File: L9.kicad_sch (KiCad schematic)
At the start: 38 parts

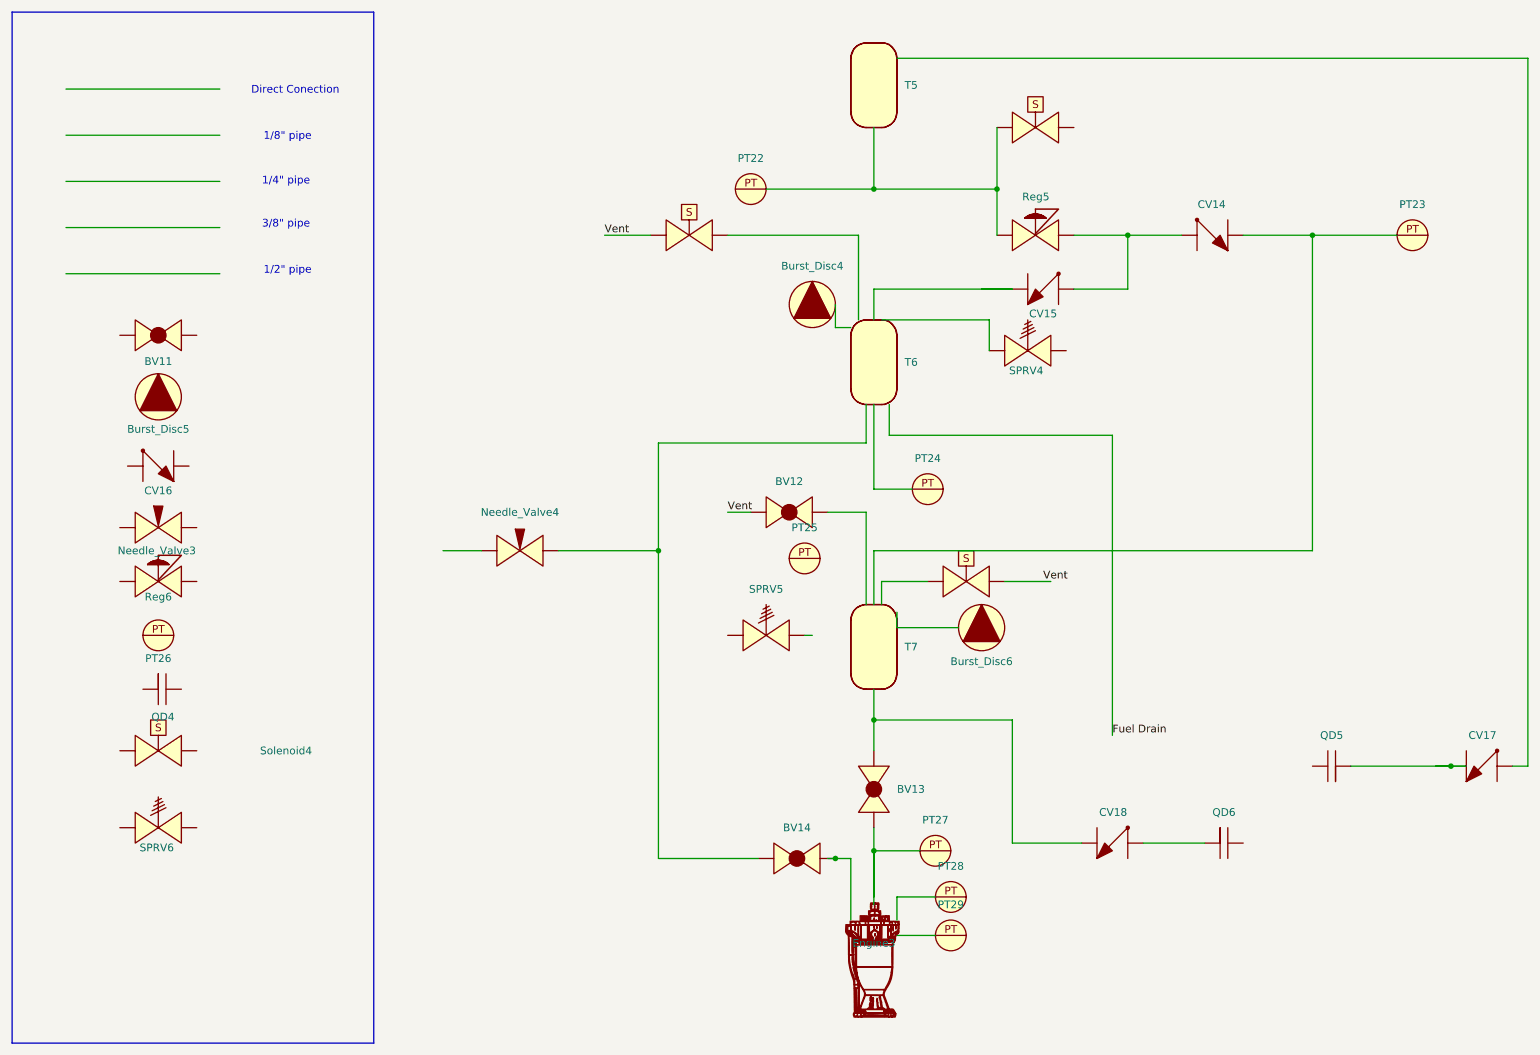
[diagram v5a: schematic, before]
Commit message: Added Igniter + Hopper Engine test
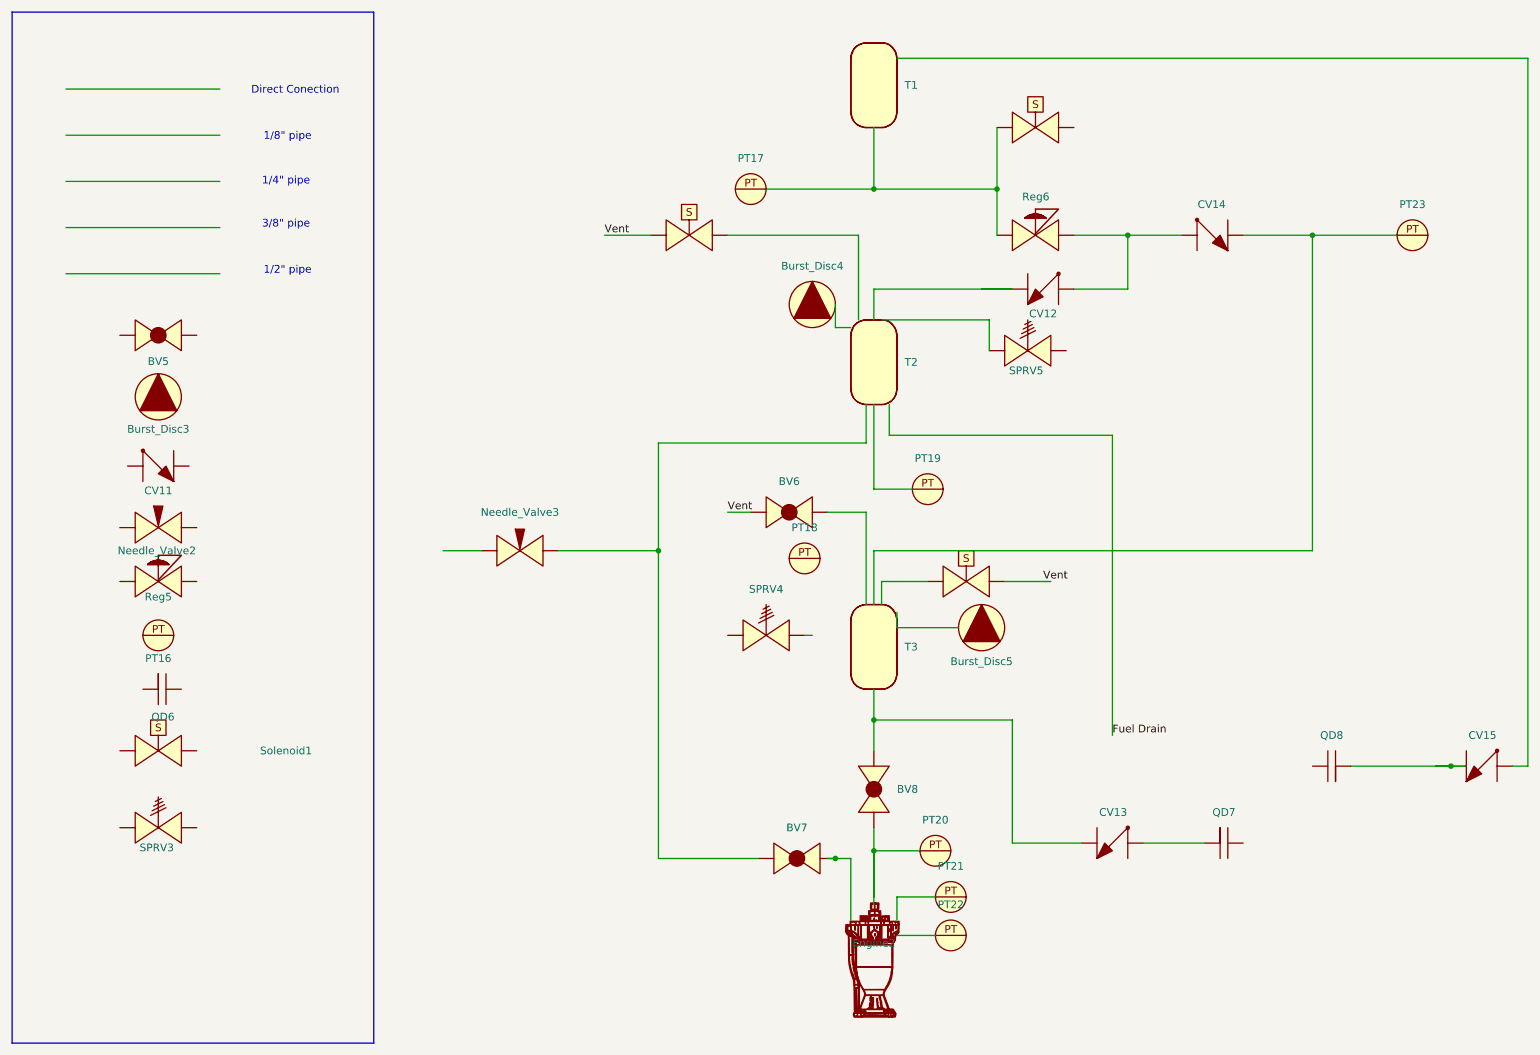
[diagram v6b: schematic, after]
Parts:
- renumbered BV11 to BV5, BV12 to BV6, BV14 to BV7, BV13 to BV8, Burst_Disc5 to Burst_Disc3, Burst_Disc6 to Burst_Disc5, CV16 to CV11, CV15 to CV12, CV18 to CV13, CV17 to CV15, Engine3 to Engine2, Needle_Valve3 to Needle_Valve2, Needle_Valve4 to Needle_Valve3, PT26 to PT16, PT22 to PT17, PT25 to PT18, PT24 to PT19, PT27 to PT20, PT28 to PT21, PT29 to PT22, QD4 to QD6, QD6 to QD7, QD5 to QD8, Reg6 to Reg5, Reg5 to Reg6, SPRV6 to SPRV3, SPRV5 to SPRV4, SPRV4 to SPRV5, Solenoid4 to Solenoid1, Solenoid1 to Solenoid4, T5 to T1, T6 to T2, T7 to T3
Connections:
- net at QD7.: now also CV13.
- net at CV13.: now also BV8., T3.; no longer QD7.
- net at PT23.: now also CV14., T3.
- net at CV15.: now also QD8.
- net at QD8.: no longer CV15.
- net at Engine2.: now also BV8., PT20.; no longer BV7.
- net at PT21.: no longer Engine2.
- net at Needle_Valve3.: now also BV7.
- new net: CV12., CV14., Reg6.
- new net: PT17., Reg6., Solenoid4., T1.
- new net: BV7., Engine2.
- new net: Engine2., PT21.
- now unconnected: PT17., PT20., Solenoid4., T1.

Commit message: overwrite
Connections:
- net at QD7.: now also CV13.
- net at CV13.: now also BV8., T3.; no longer QD7.
- net at PT23.: now also CV14., T3.
- net at CV15.: now also QD8.
- net at QD8.: no longer CV15.
- net at Engine2.: now also BV8., PT20.; no longer BV7.
- net at PT21.: no longer Engine2.
- net at Needle_Valve3.: now also BV7.
- new net: CV12., CV14., Reg6.
- new net: PT17., Reg6., Solenoid4., T1.
- new net: BV7., Engine2.
- new net: Engine2., PT21.
- now unconnected: PT17., PT20., Solenoid4., T1.
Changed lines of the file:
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@@
 	(label "Vent"
 		(at 132.08 99.06 0)
+		(fields_autoplaced yes)
 		(effects
 			(font
@@
 	(label "Fuel Drain"
 		(at 195.58 135.89 0)
+		(fields_autoplaced yes)
 		(effects
 			(font
@@
 	(label "Vent"
 		(at 111.76 53.34 0)
+		(fields_autoplaced yes)
 		(effects
 			(font
@@
 	(label "Vent"
 		(at 184.15 110.49 0)
+		(fields_autoplaced yes)
 		(effects
 			(font

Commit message: Big Pluto Commit, baboucarr jeng imperial college london second year aeronautics student.
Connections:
- net at QD7.: now also CV13.
- net at CV13.: now also BV8., T3.; no longer QD7.
- net at PT23.: now also CV14., T3.
- net at CV15.: now also QD8.
- net at QD8.: no longer CV15.
- net at Engine2.: now also BV8., PT20.; no longer BV7.
- net at PT21.: no longer Engine2.
- net at Needle_Valve3.: now also BV7.
- new net: CV12., CV14., Reg6.
- new net: PT17., Reg6., Solenoid4., T1.
- new net: BV7., Engine2.
- new net: Engine2., PT21.
- now unconnected: PT17., PT20., Solenoid4., T1.
